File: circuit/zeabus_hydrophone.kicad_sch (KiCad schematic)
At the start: 71 parts, among them CON1 ZTEX-V2-FPGA, J1 JTAG, U1 AD9248, U2 AD9248, U3 REF1933

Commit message: Re-arrange and re-route PCB with some correction
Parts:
- added C2: 0.1uF, Capacitor_SMD:C_0603_1608Metric_Pad1.08x0.95mm_HandSolder, symbol Device:C_Small
- added LED10: YEL3, LED_SMD:LED_0603_1608Metric_Pad1.05x0.95mm_HandSolder, symbol Device:LED_Small
- added LED11: GRE3, LED_SMD:LED_0603_1608Metric_Pad1.05x0.95mm_HandSolder, symbol Device:LED_Small
- added LED3: RED1, LED_SMD:LED_0603_1608Metric_Pad1.05x0.95mm_HandSolder, symbol Device:LED_Small
- added LED4: YEL1, LED_SMD:LED_0603_1608Metric_Pad1.05x0.95mm_HandSolder, symbol Device:LED_Small
- added LED5: GRE1, LED_SMD:LED_0603_1608Metric_Pad1.05x0.95mm_HandSolder, symbol Device:LED_Small
- added LED6: RED2, LED_SMD:LED_0603_1608Metric_Pad1.05x0.95mm_HandSolder, symbol Device:LED_Small
- added LED7: YEL2, LED_SMD:LED_0603_1608Metric_Pad1.05x0.95mm_HandSolder, symbol Device:LED_Small
- added LED8: GRE2, LED_SMD:LED_0603_1608Metric_Pad1.05x0.95mm_HandSolder, symbol Device:LED_Small
- added LED9: RED3, LED_SMD:LED_0603_1608Metric_Pad1.05x0.95mm_HandSolder, symbol Device:LED_Small
- added R10, R11, R3, R4, R5, R6, R7, R8, R9: 240, Resistor_SMD:R_0603_1608Metric_Pad1.05x0.95mm_HandSolder, symbol Device:R_Small_US
- C1: renamed from C50; footprint Capacitor_SMD:C_0603_1608Metric_Pad1.05x0.95mm_HandSolder -> Capacitor_SMD:C_0603_1608Metric_Pad1.08x0.95mm_HandSolder
- C10: renamed from C9; footprint Capacitor_SMD:C_0603_1608Metric_Pad1.05x0.95mm_HandSolder -> Capacitor_SMD:C_0603_1608Metric_Pad1.08x0.95mm_HandSolder
- C11: renamed from C12; footprint Capacitor_SMD:C_0603_1608Metric_Pad1.05x0.95mm_HandSolder -> Capacitor_SMD:C_0603_1608Metric_Pad1.08x0.95mm_HandSolder
- C12: renamed from C15; footprint Capacitor_SMD:C_0603_1608Metric_Pad1.05x0.95mm_HandSolder -> Capacitor_SMD:C_0603_1608Metric_Pad1.08x0.95mm_HandSolder
- C13: renamed from C18; footprint Capacitor_SMD:C_0603_1608Metric_Pad1.05x0.95mm_HandSolder -> Capacitor_SMD:C_0603_1608Metric_Pad1.08x0.95mm_HandSolder
- C14: renamed from C34; footprint Capacitor_SMD:C_0805_2012Metric_Pad1.15x1.40mm_HandSolder -> Capacitor_SMD:C_0805_2012Metric_Pad1.18x1.45mm_HandSolder
- C15: renamed from C37; footprint Capacitor_SMD:C_0805_2012Metric_Pad1.15x1.40mm_HandSolder -> Capacitor_SMD:C_0805_2012Metric_Pad1.18x1.45mm_HandSolder
- C16: renamed from C40; footprint Capacitor_SMD:C_0805_2012Metric_Pad1.15x1.40mm_HandSolder -> Capacitor_SMD:C_0805_2012Metric_Pad1.18x1.45mm_HandSolder
- C17: renamed from C10; footprint Capacitor_SMD:C_0805_2012Metric_Pad1.15x1.40mm_HandSolder -> Capacitor_SMD:C_0805_2012Metric_Pad1.18x1.45mm_HandSolder
- C18: renamed from C13; footprint Capacitor_SMD:C_0805_2012Metric_Pad1.15x1.40mm_HandSolder -> Capacitor_SMD:C_0805_2012Metric_Pad1.18x1.45mm_HandSolder
- C19: renamed from C16; footprint Capacitor_SMD:C_0805_2012Metric_Pad1.15x1.40mm_HandSolder -> Capacitor_SMD:C_0805_2012Metric_Pad1.18x1.45mm_HandSolder
- C20: renamed from C49; footprint Capacitor_SMD:C_0603_1608Metric_Pad1.05x0.95mm_HandSolder -> Capacitor_SMD:C_0603_1608Metric_Pad1.08x0.95mm_HandSolder
- C21: renamed from C44; footprint Capacitor_SMD:C_0603_1608Metric_Pad1.05x0.95mm_HandSolder -> Capacitor_SMD:C_0603_1608Metric_Pad1.08x0.95mm_HandSolder
- C22: renamed from C20; footprint Capacitor_SMD:C_0603_1608Metric_Pad1.05x0.95mm_HandSolder -> Capacitor_SMD:C_0603_1608Metric_Pad1.08x0.95mm_HandSolder
- C23: renamed from C35; footprint Capacitor_SMD:C_0603_1608Metric_Pad1.05x0.95mm_HandSolder -> Capacitor_SMD:C_0603_1608Metric_Pad1.08x0.95mm_HandSolder
- C24: renamed from C38; footprint Capacitor_SMD:C_0603_1608Metric_Pad1.05x0.95mm_HandSolder -> Capacitor_SMD:C_0603_1608Metric_Pad1.08x0.95mm_HandSolder
- C25: renamed from C41; footprint Capacitor_SMD:C_0603_1608Metric_Pad1.05x0.95mm_HandSolder -> Capacitor_SMD:C_0603_1608Metric_Pad1.08x0.95mm_HandSolder
- C26: renamed from C11; footprint Capacitor_SMD:C_0603_1608Metric_Pad1.05x0.95mm_HandSolder -> Capacitor_SMD:C_0603_1608Metric_Pad1.08x0.95mm_HandSolder
- C27: renamed from C14; footprint Capacitor_SMD:C_0603_1608Metric_Pad1.05x0.95mm_HandSolder -> Capacitor_SMD:C_0603_1608Metric_Pad1.08x0.95mm_HandSolder
- C28: renamed from C17; footprint Capacitor_SMD:C_0603_1608Metric_Pad1.05x0.95mm_HandSolder -> Capacitor_SMD:C_0603_1608Metric_Pad1.08x0.95mm_HandSolder
- C29: renamed from C45; footprint Capacitor_SMD:C_0603_1608Metric_Pad1.05x0.95mm_HandSolder -> Capacitor_SMD:C_0603_1608Metric_Pad1.08x0.95mm_HandSolder
- C3: renamed from C51; footprint Capacitor_SMD:C_0603_1608Metric_Pad1.05x0.95mm_HandSolder -> Capacitor_SMD:C_0603_1608Metric_Pad1.08x0.95mm_HandSolder
- C30: renamed from C21; footprint Capacitor_SMD:C_0603_1608Metric_Pad1.05x0.95mm_HandSolder -> Capacitor_SMD:C_0603_1608Metric_Pad1.08x0.95mm_HandSolder
- C31: renamed from C46; footprint Capacitor_SMD:C_0603_1608Metric_Pad1.05x0.95mm_HandSolder -> Capacitor_SMD:C_0603_1608Metric_Pad1.08x0.95mm_HandSolder
- C32: renamed from C22; footprint Capacitor_SMD:C_0603_1608Metric_Pad1.05x0.95mm_HandSolder -> Capacitor_SMD:C_0603_1608Metric_Pad1.08x0.95mm_HandSolder
- C33: renamed from C25; footprint Capacitor_SMD:C_0603_1608Metric_Pad1.05x0.95mm_HandSolder -> Capacitor_SMD:C_0603_1608Metric_Pad1.08x0.95mm_HandSolder
- C34: renamed from C1; footprint Capacitor_SMD:C_0603_1608Metric_Pad1.05x0.95mm_HandSolder -> Capacitor_SMD:C_0603_1608Metric_Pad1.08x0.95mm_HandSolder
- C35: renamed from C47; footprint Capacitor_SMD:C_0603_1608Metric_Pad1.05x0.95mm_HandSolder -> Capacitor_SMD:C_0603_1608Metric_Pad1.08x0.95mm_HandSolder
- C36: renamed from C23; footprint Capacitor_SMD:C_0603_1608Metric_Pad1.05x0.95mm_HandSolder -> Capacitor_SMD:C_0603_1608Metric_Pad1.08x0.95mm_HandSolder
- C37: renamed from C26; footprint Capacitor_SMD:C_0603_1608Metric_Pad1.05x0.95mm_HandSolder -> Capacitor_SMD:C_0603_1608Metric_Pad1.08x0.95mm_HandSolder
- C38: renamed from C2; footprint Capacitor_SMD:C_0603_1608Metric_Pad1.05x0.95mm_HandSolder -> Capacitor_SMD:C_0603_1608Metric_Pad1.08x0.95mm_HandSolder
- C39: renamed from C48; footprint Capacitor_SMD:C_0603_1608Metric_Pad1.05x0.95mm_HandSolder -> Capacitor_SMD:C_0603_1608Metric_Pad1.08x0.95mm_HandSolder
- C4: renamed from C43; footprint Capacitor_SMD:C_0603_1608Metric_Pad1.05x0.95mm_HandSolder -> Capacitor_SMD:C_0603_1608Metric_Pad1.08x0.95mm_HandSolder
- C40: renamed from C24; footprint Capacitor_SMD:C_0603_1608Metric_Pad1.05x0.95mm_HandSolder -> Capacitor_SMD:C_0603_1608Metric_Pad1.08x0.95mm_HandSolder
- C41: renamed from C27; footprint Capacitor_SMD:C_0603_1608Metric_Pad1.05x0.95mm_HandSolder -> Capacitor_SMD:C_0603_1608Metric_Pad1.08x0.95mm_HandSolder
- C42: renamed from C3; footprint Capacitor_SMD:C_0603_1608Metric_Pad1.05x0.95mm_HandSolder -> Capacitor_SMD:C_0603_1608Metric_Pad1.08x0.95mm_HandSolder
- C43: renamed from C28; footprint Capacitor_SMD:C_0603_1608Metric_Pad1.05x0.95mm_HandSolder -> Capacitor_SMD:C_0603_1608Metric_Pad1.08x0.95mm_HandSolder
- C44: renamed from C4; footprint Capacitor_SMD:C_0603_1608Metric_Pad1.05x0.95mm_HandSolder -> Capacitor_SMD:C_0603_1608Metric_Pad1.08x0.95mm_HandSolder
- C45: renamed from C29; footprint Capacitor_SMD:C_0603_1608Metric_Pad1.05x0.95mm_HandSolder -> Capacitor_SMD:C_0603_1608Metric_Pad1.08x0.95mm_HandSolder
- C46: renamed from C5; footprint Capacitor_SMD:C_0603_1608Metric_Pad1.05x0.95mm_HandSolder -> Capacitor_SMD:C_0603_1608Metric_Pad1.08x0.95mm_HandSolder
- C47: renamed from C30; footprint Capacitor_SMD:C_0603_1608Metric_Pad1.05x0.95mm_HandSolder -> Capacitor_SMD:C_0603_1608Metric_Pad1.08x0.95mm_HandSolder
- C48: renamed from C6; footprint Capacitor_SMD:C_0603_1608Metric_Pad1.05x0.95mm_HandSolder -> Capacitor_SMD:C_0603_1608Metric_Pad1.08x0.95mm_HandSolder
- C49: renamed from C31; footprint Capacitor_SMD:C_0603_1608Metric_Pad1.05x0.95mm_HandSolder -> Capacitor_SMD:C_0603_1608Metric_Pad1.08x0.95mm_HandSolder
- C5: renamed from C19; footprint Capacitor_SMD:C_0603_1608Metric_Pad1.05x0.95mm_HandSolder -> Capacitor_SMD:C_0603_1608Metric_Pad1.08x0.95mm_HandSolder
- C50: renamed from C7; footprint Capacitor_SMD:C_0603_1608Metric_Pad1.05x0.95mm_HandSolder -> Capacitor_SMD:C_0603_1608Metric_Pad1.08x0.95mm_HandSolder
- C51: renamed from C32; footprint Capacitor_SMD:C_0603_1608Metric_Pad1.05x0.95mm_HandSolder -> Capacitor_SMD:C_0603_1608Metric_Pad1.08x0.95mm_HandSolder
- C52: renamed from C8; footprint Capacitor_SMD:C_0603_1608Metric_Pad1.05x0.95mm_HandSolder -> Capacitor_SMD:C_0603_1608Metric_Pad1.08x0.95mm_HandSolder
- C6: renamed from C33; footprint Capacitor_SMD:C_0603_1608Metric_Pad1.05x0.95mm_HandSolder -> Capacitor_SMD:C_0603_1608Metric_Pad1.08x0.95mm_HandSolder
- C7: renamed from C36; footprint Capacitor_SMD:C_0603_1608Metric_Pad1.05x0.95mm_HandSolder -> Capacitor_SMD:C_0603_1608Metric_Pad1.08x0.95mm_HandSolder
- C8: renamed from C39; footprint Capacitor_SMD:C_0603_1608Metric_Pad1.05x0.95mm_HandSolder -> Capacitor_SMD:C_0603_1608Metric_Pad1.08x0.95mm_HandSolder
- C9: renamed from C42; footprint Capacitor_SMD:C_0603_1608Metric_Pad1.05x0.95mm_HandSolder -> Capacitor_SMD:C_0603_1608Metric_Pad1.08x0.95mm_HandSolder
- renumbered LED2 to LED1, LED1 to LED2, R54 to R12, R53 to R13
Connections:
- net GNDA: now also C2.1, LED10.1 (K), LED11.1 (K), LED3.1 (K), LED4.1 (K), LED5.1 (K), LED6.1 (K), LED7.1 (K), LED8.1 (K), LED9.1 (K)
- net GNDREF: now also C2.2
- net at RN6.5 (R4.2): now also CON1.A22 (IO-C15); no longer CON1.C10 (IO-T6)
- net at RN7.8 (R1.2): now also CON1.A23 (IO-B17); no longer CON1.C11 (IO-R6)
- net at CON1.C12 (IO-R5): now also RN1.8 (R1.2); no longer RN7.7 (R2.2)
- net at CON1.C13 (IO-V2): now also RN1.7 (R2.2); no longer RN7.6 (R3.2)
- net at CON1.C14 (IO-U2): now also RN1.6 (R3.2); no longer RN7.5 (R4.2)
- net at CON1.C15 (IO-K6): now also RN1.5 (R4.2); no longer RN8.8 (R1.2)
- net at CON1.C19 (IO-N6): now also RN2.8 (R1.2); no longer RN8.7 (R2.2)
- net at CON1.C20 (IO-M6): now also RN2.7 (R2.2); no longer RN8.6 (R3.2)
- net at CON1.C21 (IO-L6): now also RN2.6 (R3.2); no longer RN8.5 (R4.2)
- net at CON1.C22 (IO-L5): now also RN2.5 (R4.2); no longer R2.1
- net at CON1.C23 (IO-N4): now also RN3.8 (R1.2)
- net at CON1.C24 (IO-M4): now also RN3.7 (R2.2)
- net at CON1.C25 (IO-M3): now also RN3.6 (R3.2)
- net at CON1.C26 (IO-M2): now also RN3.5 (R4.2)
- net at CON1.C27 (IO-K5): now also RN4.8 (R1.2)
- net at CON1.C28 (IO-L4): now also RN4.7 (R2.2)
- net at CON1.C29 (IO-L3): now also RN4.6 (R3.2)
- net at RN5.8 (R1.2): now also CON1.A12 (IO-E18); no longer CON1.C3 (IO-U9)
- net at CON1.C30 (IO-K3): now also RN4.5 (R4.2)
- net at RN5.7 (R2.2): now also CON1.A13 (IO-D18); no longer CON1.C4 (IO-U8)
- net at RN5.6 (R3.2): now also CON1.A14 (IO-G13); no longer CON1.C5 (IO-U7)
- net at RN5.5 (R4.2): now also CON1.A18 (IO-F13); no longer CON1.C6 (IO-U6)
- net at RN6.8 (R1.2): now also CON1.A19 (IO-E16); no longer CON1.C7 (IO-T8)
- net at RN6.7 (R2.2): now also CON1.A20 (IO-C17); no longer CON1.C8 (IO-R8)
- net at RN6.6 (R3.2): now also CON1.A21 (IO-A18); no longer CON1.C9 (IO-R7)
- net at CON1.D11 (IO-U3): now also R12.1
- net at CON1.D12 (IO-V1): now also R13.1
- net at CON1.D20 (IO-N5): now also R3.2
- net at CON1.D21 (IO-P4): now also R4.2
- net at CON1.D22 (IO-P3): now also R5.2
- net at CON1.D23 (IO-T1): now also R6.2
- net at CON1.D24 (IO-R1): now also R7.2
- net at CON1.D25 (IO-R2): now also R8.2
- net at CON1.D26 (IO-P2): now also R9.2
- net at CON1.D27 (IO-N2): now also R10.2
- net at CON1.D28 (IO-N1): now also R11.2
- net at CON1.A10 (IO-G18): no longer RN2.5 (R4.2)
- net at CON1.A11 (IO-F18): now also R2.1; no longer RN3.8 (R1.2)
- net at R1.1: now also CON1.C11 (IO-R6); no longer CON1.A22 (IO-C15)
- net at CON1.A24 (IO-C14): now also RN7.7 (R2.2)
- net at CON1.A25 (IO-D13): now also RN7.6 (R3.2)
- net at CON1.A26 (IO-A16): now also RN7.5 (R4.2)
- net at CON1.A27 (IO-B14): now also RN8.8 (R1.2)
- net at CON1.A28 (IO-B12): now also RN8.7 (R2.2)
- net at CON1.A29 (IO-A14): now also RN8.6 (R3.2)
- net at CON1.A3 (IO-K16): no longer RN1.8 (R1.2)
- net at CON1.A30 (IO-B11): now also RN8.5 (R4.2)
- net at CON1.A4 (IO-K15): no longer RN1.7 (R2.2)
- net at CON1.A5 (IO-J15): no longer RN1.6 (R3.2)
- net at CON1.A6 (IO-H15): no longer RN1.5 (R4.2)
- net at CON1.A7 (IO-J14): no longer RN2.8 (R1.2)
- net at CON1.A8 (IO-H17): no longer RN2.7 (R2.2)
- net at CON1.A9 (IO-G17): no longer RN2.6 (R3.2)
- net at CON1.B13 (IO-E17): no longer R13.1
- net at CON1.B14 (IO-D17): no longer R12.1
- new net: LED10.2 (A), R10.1
- new net: LED9.2 (A), R9.1
- new net: LED7.2 (A), R7.1
- new net: LED3.2 (A), R3.1
- new net: LED6.2 (A), R6.1
- new net: LED11.2 (A), R11.1
- new net: LED8.2 (A), R8.1
- new net: LED4.2 (A), R4.1
- new net: LED5.2 (A), R5.1
- no-connect marks 101 -> 81
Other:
- company: Zeabus AUV Team -> SEAPUP AUV Team
- moved on the sheet: C1, C3, CON1C, FB1, LED1, LED2, R1, R12, R13, R2, RN1, RN2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

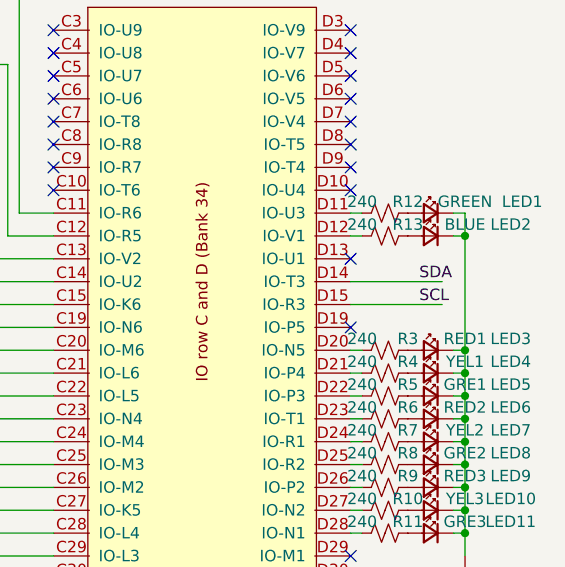
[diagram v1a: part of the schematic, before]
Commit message: Change FPGA-board socket from THT to SMD
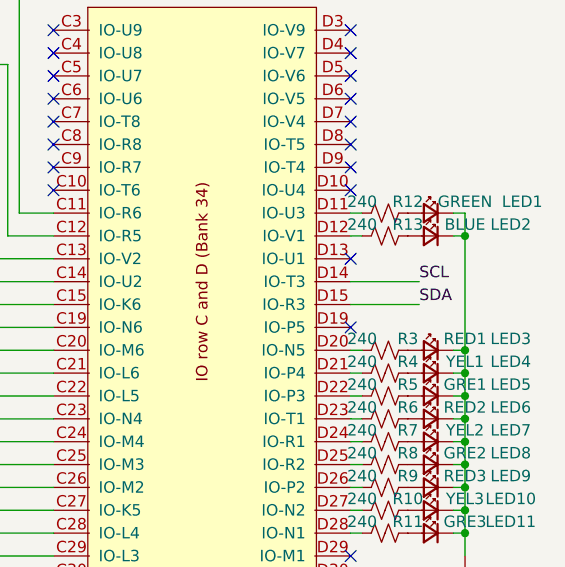
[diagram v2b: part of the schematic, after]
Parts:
- CON1: footprint zeabus:ZTEX-V2-FPGA -> zeabus:ZTEX-V2-FPGA-SMD
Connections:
- net SCL: now also CON1.D14 (IO-T3); no longer CON1.D15 (IO-R3)
- net SDA: now also CON1.D15 (IO-R3); no longer CON1.D14 (IO-T3)
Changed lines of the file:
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@@
     (stroke (width 0) (type default) (color 0 0 0 0))
   )
+  (wire (pts (xy 265.43 57.15) (xy 273.05 57.15))
+    (stroke (width 0) (type default) (color 0 0 0 0))
+  )
   (wire (pts (xy 278.13 64.77) (xy 278.13 62.23))
     (stroke (width 0) (type default) (color 0 0 0 0))
@@
     (stroke (width 0) (type default) (color 0 0 0 0))
   )
-  (wire (pts (xy 265.43 54.61) (xy 275.59 54.61))
-    (stroke (width 0) (type default) (color 0 0 0 0))
-  )
   (wire (pts (xy 165.1 170.18) (xy 165.1 172.72))
     (stroke (width 0) (type default) (color 0 0 0 0))
@@
     (stroke (width 0) (type default) (color 0 0 0 0))
   )
-  (wire (pts (xy 265.43 57.15) (xy 275.59 57.15))
-    (stroke (width 0) (type default) (color 0 0 0 0))
-  )
   (wire (pts (xy 68.58 116.84) (xy 59.69 116.84))
     (stroke (width 0) (type default) (color 0 0 0 0))
@@
     (stroke (width 0) (type default) (color 0 0 0 0))
   )
+  (wire (pts (xy 265.43 54.61) (xy 273.05 54.61))
+    (stroke (width 0) (type default) (color 0 0 0 0))
+  )
   (wire (pts (xy 203.2 54.61) (xy 203.2 58.42))
     (stroke (width 0) (type default) (color 0 0 0 0))
@@
     (effects (font (size 1.27 1.27)) (justify right bottom))
   )
-  (label "SCL" (at 273.05 57.15 0)
+  (label "SCL" (at 273.05 54.61 0)
     (effects (font (size 1.27 1.27)) (justify left bottom))
   )
@@
     (effects (font (size 1.27 1.27)) (justify right bottom))
   )
-  (label "SDA" (at 273.05 54.61 0)
+  (label "SDA" (at 273.05 57.15 0)
     (effects (font (size 1.27 1.27)) (justify left bottom))
   )
@@
     (property "Reference" "CON1" (id 0) (at 147.955 146.939 0))
     (property "Value" "ZTEX-V2-FPGA" (id 1) (at 147.955 149.2504 0))
-    (property "Footprint" "zeabus:ZTEX-V2-FPGA" (id 2) (at 175.26 201.93 0)
+    (property "Footprint" "zeabus:ZTEX-V2-FPGA-SMD" (id 2) (at 175.26 201.93 0)
       (effects (font (size 1.27 1.27)) hide)
     )
@@
       (effects (font (size 1.27 1.27)) (justify left))
     )
-    (property "Footprint" "zeabus:ZTEX-V2-FPGA" (id 2) (at 140.97 208.28 0)
+    (property "Footprint" "zeabus:ZTEX-V2-FPGA-SMD" (id 2) (at 140.97 208.28 0)
       (effects (font (size 1.27 1.27)) hide)
     )
@@
     (property "Reference" "CON1" (id 0) (at 248.92 19.939 0))
     (property "Value" "ZTEX-V2-FPGA" (id 1) (at 248.92 22.2504 0))
-    (property "Footprint" "zeabus:ZTEX-V2-FPGA" (id 2) (at 275.59 74.93 0)
+    (property "Footprint" "zeabus:ZTEX-V2-FPGA-SMD" (id 2) (at 275.59 74.93 0)
       (effects (font (size 1.27 1.27)) hide)
     )
@@
     (property "Reference" "CON1" (id 0) (at 248.92 92.329 0))
     (property "Value" "ZTEX-V2-FPGA" (id 1) (at 248.92 94.6404 0))
-    (property "Footprint" "zeabus:ZTEX-V2-FPGA" (id 2) (at 275.59 147.32 0)
+    (property "Footprint" "zeabus:ZTEX-V2-FPGA-SMD" (id 2) (at 275.59 147.32 0)
       (effects (font (size 1.27 1.27)) hide)
     )
@@
     )
     (path "/f3c44293-9498-4250-bc18-46fd6a680a12"
-      (reference "CON1") (unit 1) (value "ZTEX-V2-FPGA") (footprint "zeabus:ZTEX-V2-FPGA")
+      (reference "CON1") (unit 1) (value "ZTEX-V2-FPGA") (footprint "zeabus:ZTEX-V2-FPGA-SMD")
     )
     (path "/4ebaa8d3-3d9d-4998-833f-093b926a0d22"
-      (reference "CON1") (unit 2) (value "ZTEX-V2-FPGA") (footprint "zeabus:ZTEX-V2-FPGA")
+      (reference "CON1") (unit 2) (value "ZTEX-V2-FPGA") (footprint "zeabus:ZTEX-V2-FPGA-SMD")
     )
     (path "/00000000-0000-0000-0000-00005dcedf09"
-      (reference "CON1") (unit 3) (value "ZTEX-V2-FPGA") (footprint "zeabus:ZTEX-V2-FPGA")
+      (reference "CON1") (unit 3) (value "ZTEX-V2-FPGA") (footprint "zeabus:ZTEX-V2-FPGA-SMD")
     )
     (path "/00000000-0000-0000-0000-00005de05739"
-      (reference "CON1") (unit 4) (value "ZTEX-V2-FPGA") (footprint "zeabus:ZTEX-V2-FPGA")
+      (reference "CON1") (unit 4) (value "ZTEX-V2-FPGA") (footprint "zeabus:ZTEX-V2-FPGA-SMD")
     )
     (path "/00000000-0000-0000-0000-00005ff2096a"
